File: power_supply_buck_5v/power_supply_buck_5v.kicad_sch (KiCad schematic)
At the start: 5 parts, among them U1 LM2596S-5

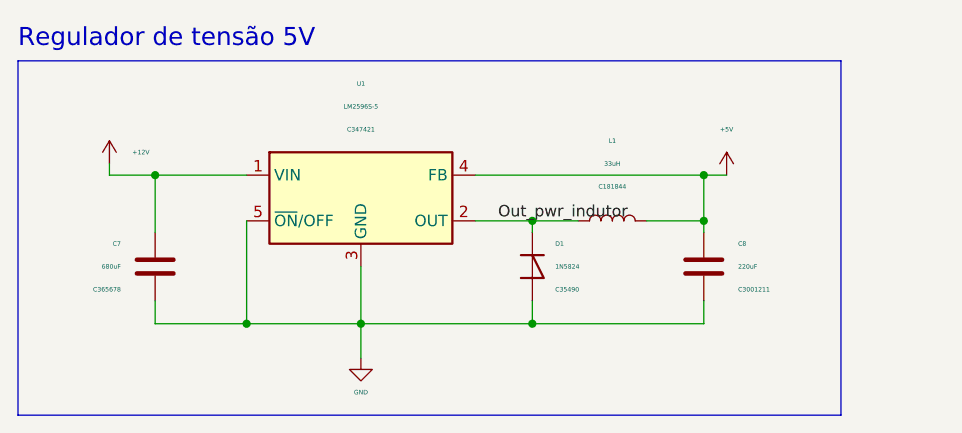
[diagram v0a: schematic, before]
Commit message: changes power_supply_buck_5v add layout
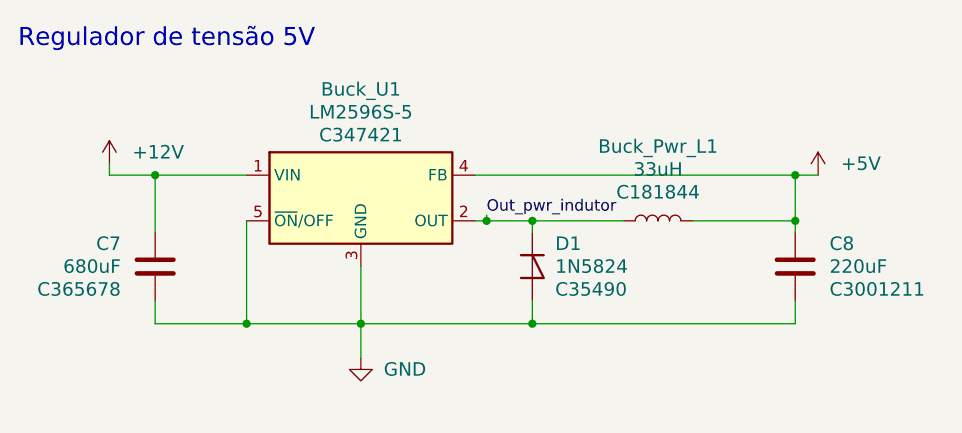
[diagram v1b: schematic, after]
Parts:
- renumbered L1 to Buck_Pwr_L1, U1 to Buck_U1
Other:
- moved on the sheet: Buck_Pwr_L1, C8
